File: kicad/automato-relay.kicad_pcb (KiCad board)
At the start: 2 copper layers, 308 x 75 mm, 47 parts, among them J1 TE-3-213598-4, J2 Screw_Terminal_01x03, J3 TE-3-213598-4, J4 Screw_Terminal_01x05, J5 TE-3-213598-4, J6 TE-3-213598-4, J7 Screw_Terminal_01x05, J8 TE-3-213598-4, K1 G5LE-14, K2 G5LE-14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

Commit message: layout: add silkscreen pin labels for J4 and J7
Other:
- board text added: "3V3"
- board text added: "CLK"
- board text added: "GND"
- board text added: "LATCH"
- board text added: "NC"
- board text added: "SDI"
- board text added: "SDO"

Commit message: add decoupling capacitors for the 74HC595
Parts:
- added C5: 10 uF, Capacitor_SMD:C_1206_3216Metric, F.Cu at (80.5, 126.2)
- added C6: 0.1 uF, Capacitor_SMD:C_1206_3216Metric, F.Cu at (80.5, 129.0)
- J4, J7: footprint Connector_Phoenix_MC_HighVoltage:PhoenixContact_MC_1,5_5-G-5.08_1x05_P5.08mm_Horizontal -> automato-relay:PhoenixContact_1935190_1x5
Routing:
- net 3V3: track 81.1 -> 86.1 mm

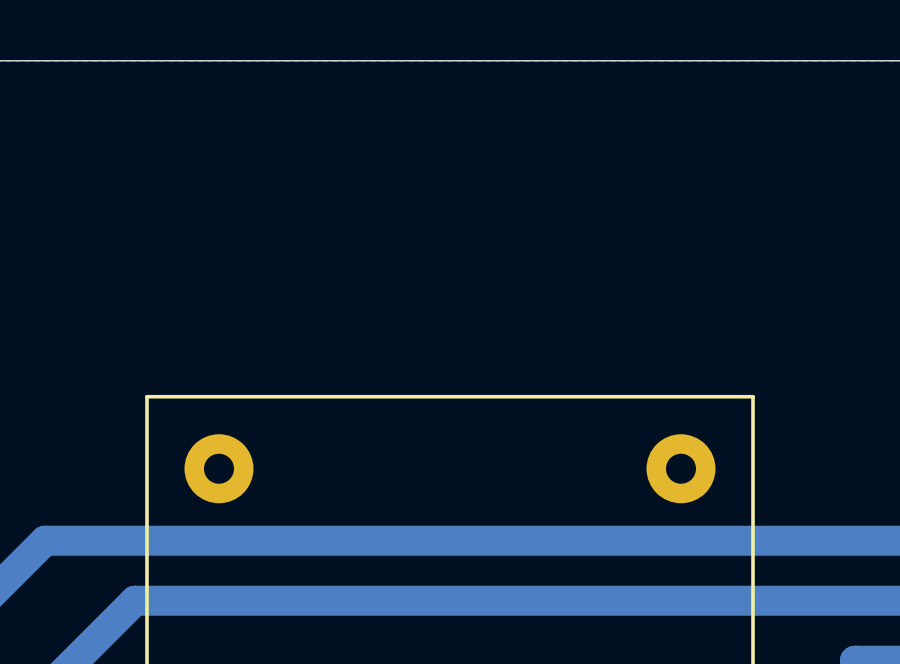
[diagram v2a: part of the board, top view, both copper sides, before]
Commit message: add decoupling capacitor for the HLK-PM03
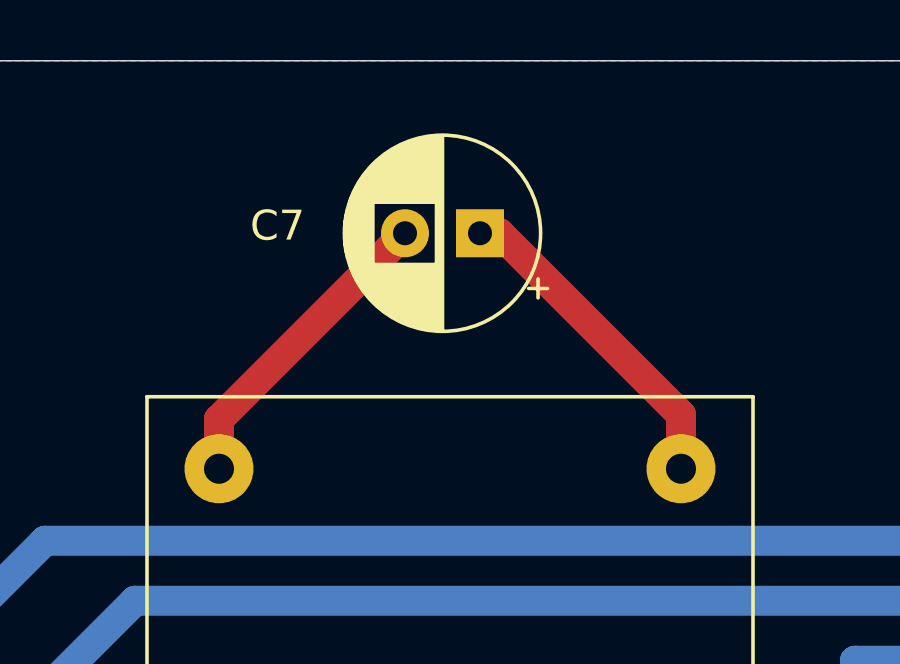
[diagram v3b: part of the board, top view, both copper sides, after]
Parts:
- added C7: 220 uF, Capacitor_THT:CP_Radial_D6.3mm_P2.50mm, F.Cu at (51.5, 102.8)
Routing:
- net 3V3: track 86.1 -> 97.1 mm
- net GND: track 71.9 -> 82.3 mm

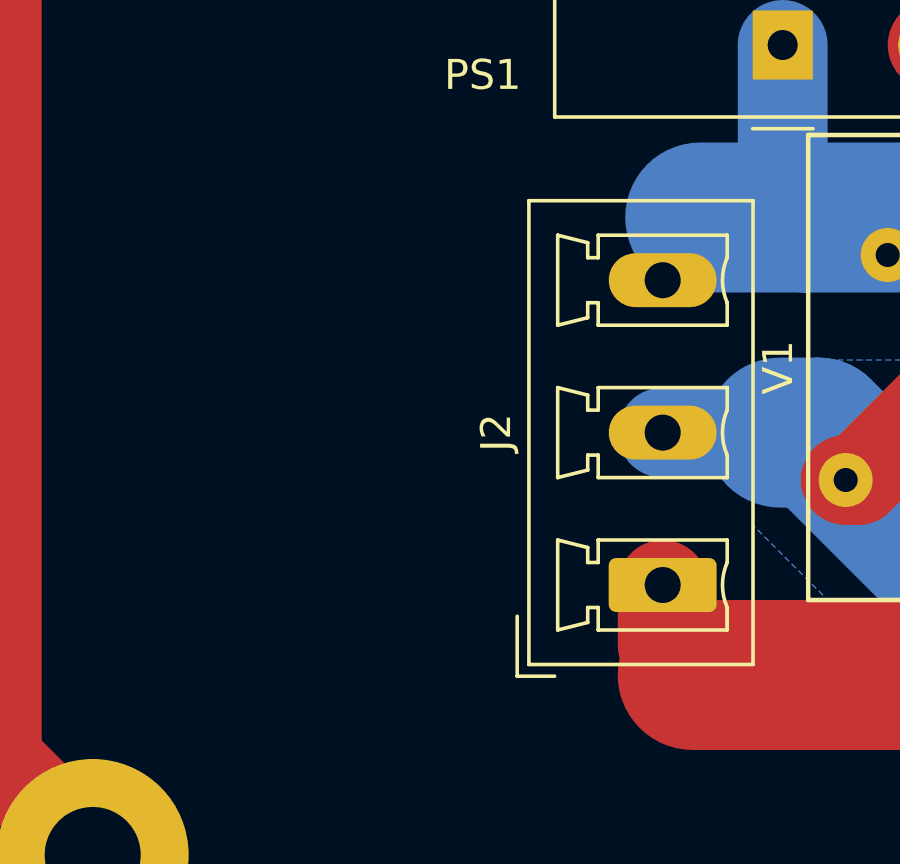
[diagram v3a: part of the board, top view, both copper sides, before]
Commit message: add X1 safety capacitor across AC lines
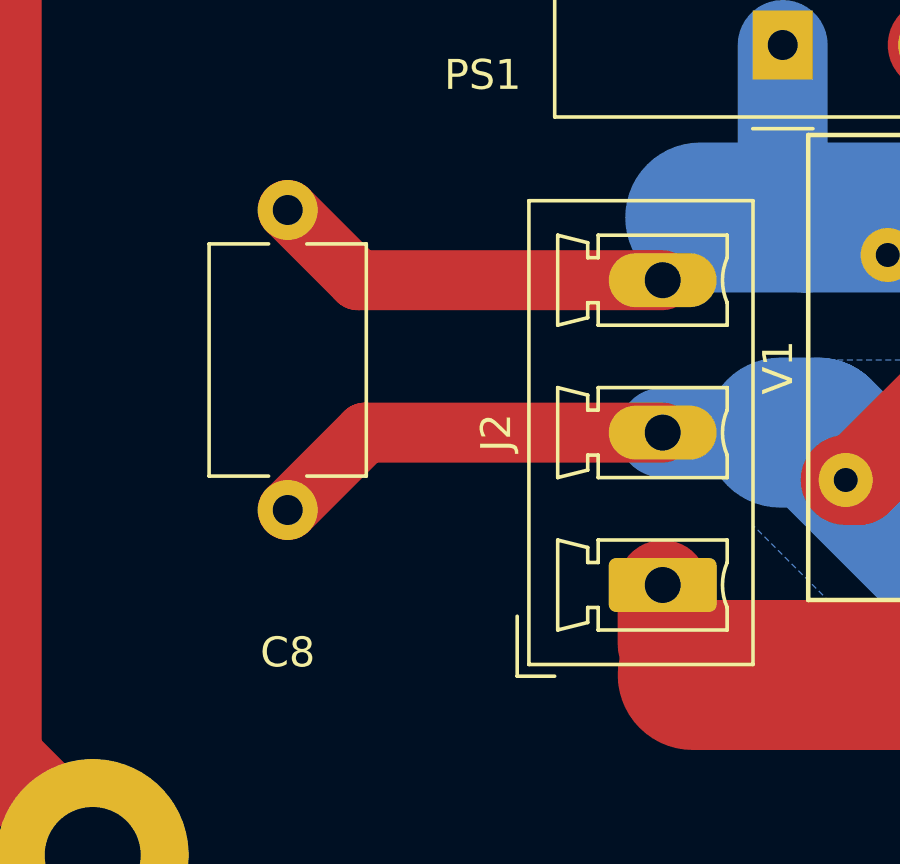
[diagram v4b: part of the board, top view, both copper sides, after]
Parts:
- added C8: 1 nF, Capacitor_THT:C_Disc_D7.5mm_W5.0mm_P10.00mm, F.Cu at (31.5, 145.5)
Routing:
- net ACN: track 425.1 -> 438.7 mm
- net ACL: track 70.6 -> 84.0 mm
